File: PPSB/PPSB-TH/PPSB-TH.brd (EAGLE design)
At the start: 17.8 x 24.1 mm, 4 parts

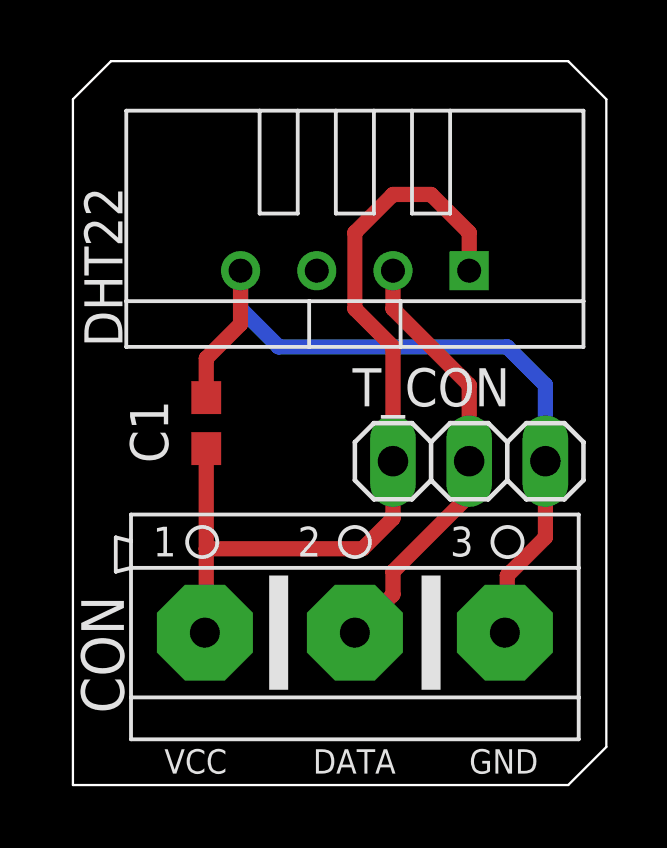
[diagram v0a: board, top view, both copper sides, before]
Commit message: Updated PPSB-T  & PPSB-TH schematics. Add PanelBoard v1.
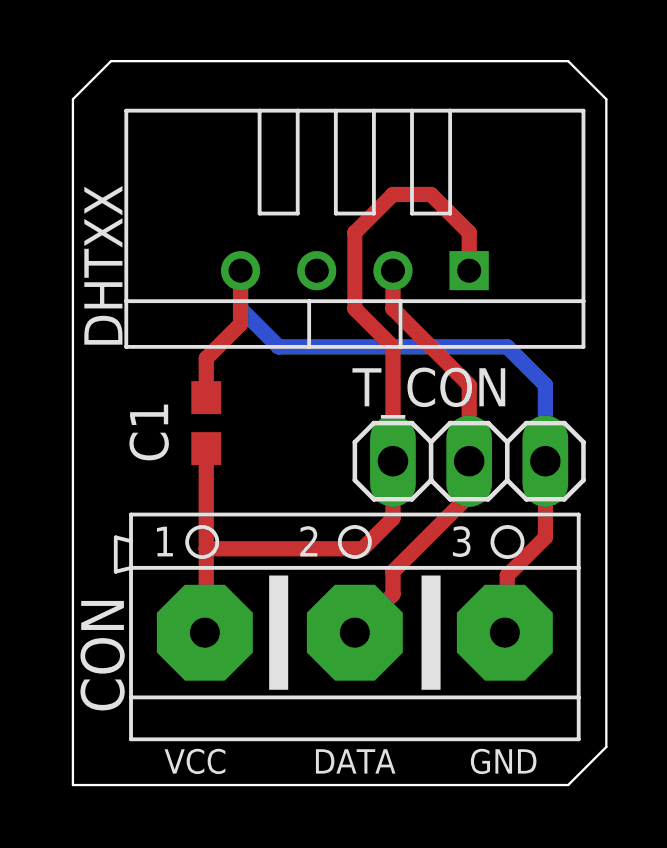
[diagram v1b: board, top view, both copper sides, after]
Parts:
- DHTXX: value DHT22 -> DHTxx
- renumbered DHT22 to DHTXX
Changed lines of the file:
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@@
 <drawing>
 <settings>
-<setting alwaysvectorfont="no"/>
+<setting alwaysvectorfont="yes"/>
 <setting verticaltext="up"/>
 </settings>
@@
 </layers>
 <board>
-<fusionsync huburn="a.cGVyc29uYWw6dWUyYzQ3NTBk" projecturn="a.cGVyc29uYWw6dWUyYzQ3NTBkIzIwMTkwNDA3MTg3MDM1OTI2" f3durn="urn:adsk.wipprod:dm.lineage:wZEhoLrnQRu7ESJgotOBgA" pcbguid="3260c9f6-525e-4db7-a396-79c3982f880a" lastpulledtime="2020-04-29T13:44:12Z" lastsyncedchangeguid="935ad107-84a7-cb2e-1b34-8bcf83f9e6d2" latestrevisionid="" lastsyncedrevisionid="" lastboardhashguid="f23f67d0-5ec7-e07c-fe61-ce9f4256d26c" lastpushedtime="2020-04-29T13:44:51Z" linktopcb3d="%12"/>
+<fusionsync huburn="a.YnVzaW5lc3M6Z21haWw4Mzc2MTI" projecturn="a.YnVzaW5lc3M6Z21haWw4Mzc2MTIjMjAyMDA1MDEyOTMzMTU4NTE" f3durn="urn:adsk.wipprod:dm.lineage:eGOhU9ZaTJetqrOAka7d6g" pcbguid="" lastpulledtime="" lastsyncedchangeguid="" latestrevisionid="6e06aa87-19e5-4749-870a-c30b73d97d0c" lastsyncedrevisionid="6e06aa87-19e5-4749-870a-c30b73d97d0c" lastboardhashguid="a0383d16-046c-f05c-dbf5-3be3ba1d8703" lastpushedtime="2020-05-02T09:15:21Z" linktopcb3d="%12"/>
 <plain>
 <text x="17.018" y="20.955" size="1.778" layer="26" rot="MR0">PROTOPlant</text>
@@
 <text x="8.001" y="0.381" size="0.8128" layer="25">DATA</text>
 <text x="13.208" y="0.381" size="0.8128" layer="25">GND</text>
+<wire x1="0" y1="22.86" x2="0" y2="0" width="0.0762" layer="20"/>
 <wire x1="0" y1="0" x2="16.51" y2="0" width="0.0762" layer="20"/>
 <wire x1="16.51" y1="0" x2="17.78" y2="1.27" width="0.0762" layer="20"/>
@@
 <wire x1="16.51" y1="24.13" x2="1.27" y2="24.13" width="0.0762" layer="20"/>
 <wire x1="1.27" y1="24.13" x2="0" y2="22.86" width="0.0762" layer="20"/>
-<wire x1="0" y1="22.86" x2="0" y2="0" width="0.0762" layer="20"/>
 </plain>
 <attributes>
@@
 <attribute name="VALUE" x="2.54" y="12.7" size="1.27" layer="27" rot="R270"/>
 </element>
-<element name="DHT22" library="diy-modules" package="TEMP-HUM-SENSOR-DHT22" value="DHT22" x="9.398" y="17.145" smashed="yes" rot="R180">
+<element name="DHTXX" library="diy-modules" package="TEMP-HUM-SENSOR-DHT22" override_package3d_urn="urn:adsk.eagle:package:19743369/2" override_package_urn="urn:adsk.eagle:footprint:19743370/1" value="DHTxx" x="9.398" y="17.145" smashed="yes" rot="R180">
 <attribute name="NAME" x="0.381" y="17.272" size="1.27" layer="25" rot="R270" align="bottom-center"/>
 <attribute name="VALUE" x="9.398" y="23.495" size="1.27" layer="27" rot="R180" align="top-center"/>
 </element>
-<element name="CON" library="#PaJa_konektory" package="ARK500/3" value="ARK500/3" x="9.398" y="5.08" smashed="yes">
+<element name="CON" library="#PaJa_konektory" library_urn="urn:adsk.eagle:library:19754563" package="ARK500/3" package3d_urn="urn:adsk.eagle:package:19754722/2" value="ARK500/3" x="9.398" y="5.08" smashed="yes">
 <attribute name="NAME" x="1.6993" y="2.3886" size="1.4224" layer="25" rot="R90"/>
 <attribute name="VALUE" x="6.1249" y="9.2732" size="1.27" layer="27"/>
@@
 <signals>
 <signal name="GND">
-<contactref element="DHT22" pad="4"/>
+<contactref element="DHTXX" pad="4"/>
 <contactref element="C1" pad="1"/>
 <contactref element="CON" pad="3"/>
@@
 </signal>
 <signal name="DATA_OUT">
-<contactref element="DHT22" pad="2"/>
+<contactref element="DHTXX" pad="2"/>
 <contactref element="CON" pad="2"/>
 <contactref element="T_CON" pad="2"/>
@@
 </signal>
 <signal name="+5V">
-<contactref element="DHT22" pad="1"/>
+<contactref element="DHTXX" pad="1"/>
 <contactref element="C1" pad="2"/>
 <contactref element="CON" pad="1"/>
@@
 packages will not be understood (or retained) with this version.
 </note>
+<note version="9.4" severity="warning">
+Since Version 9.4, EAGLE supports the overriding of 3D packages
+in schematics and board files. Those overridden 3d packages
+will not be understood (or retained) with this version.
+</note>
 </compatibility>
